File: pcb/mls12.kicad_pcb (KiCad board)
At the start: 4 copper layers, 130 x 40 mm, 137 parts, among them J1 MTJ-88ARX1-FSM-LG, J2 TC2070-FP, J3 SM04B-SRSS-TB, J4 JST B3B-ZR, J5 DC barrel plug, J6 JST B3B-ZR, J7 DC barrel plug, Q1 DMG3406L, Q2 DMG3406L, Q3 DMG3406L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

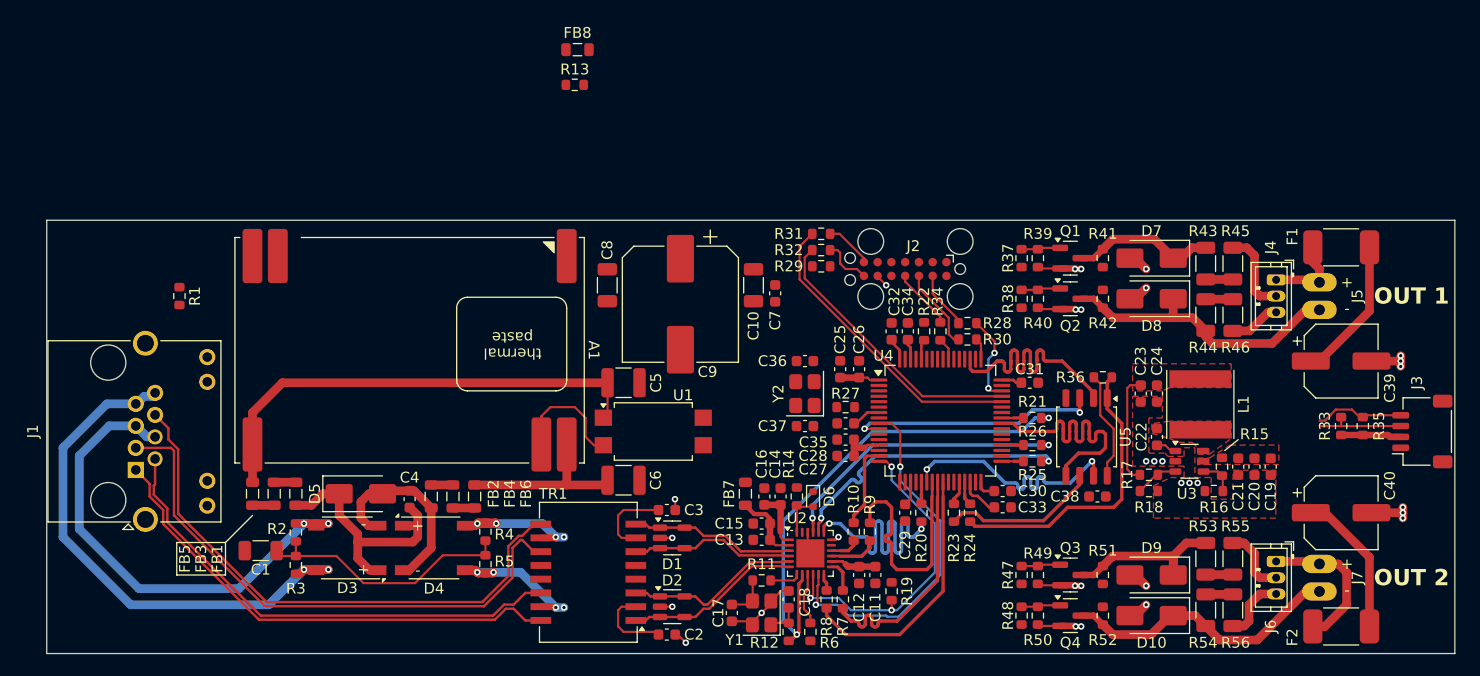
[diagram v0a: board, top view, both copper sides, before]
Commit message: Route +24V
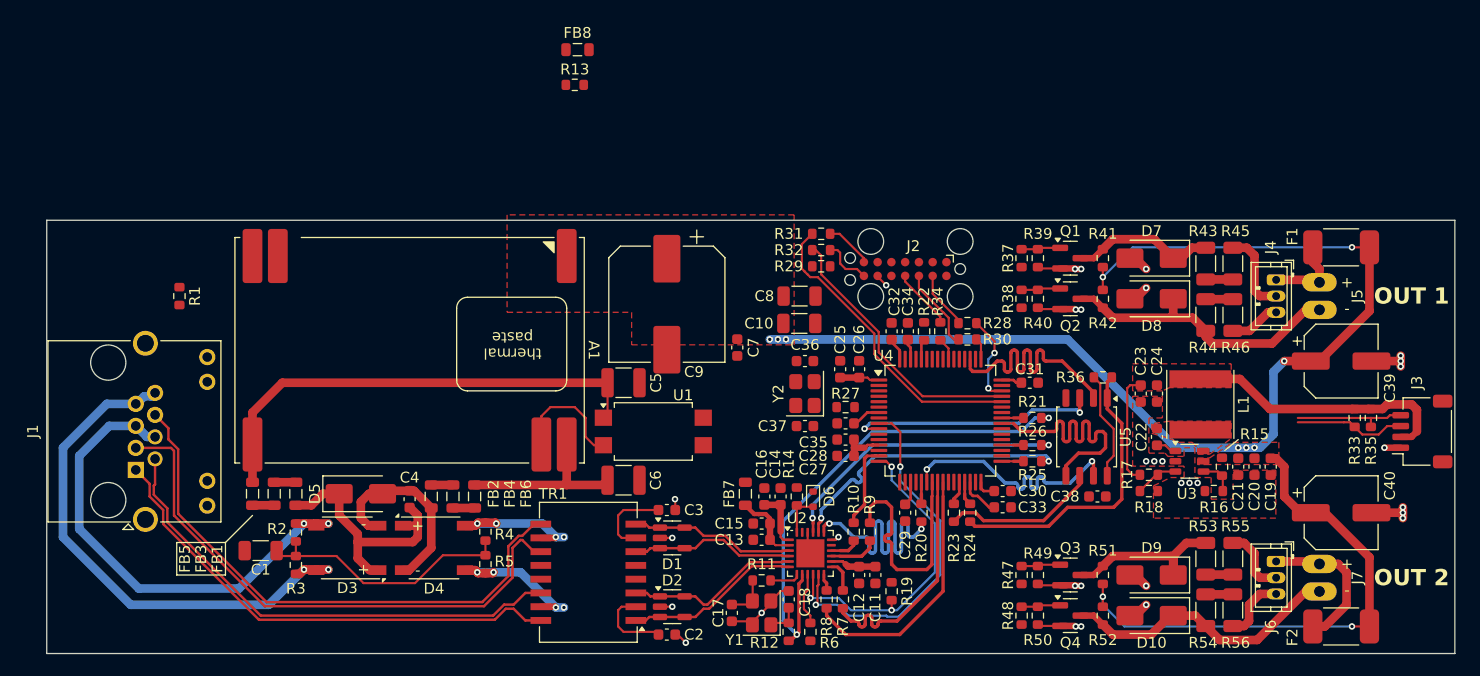
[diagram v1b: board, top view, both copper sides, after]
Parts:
- moved C8 17.8 mm to (179.5, 87.0), turned to 0 degrees
- moved C7 6.10 mm to (173.8, 91.8)
- moved C10 5.51 mm to (179.5, 89.5), turned to 0 degrees
- moved R33 1.46 mm to (230.8, 98.2), turned to -90 degrees
- moved C9 1.25 mm to (167.2, 87.8)
- moved R35 1.06 mm to (232.2, 98.2), turned to -90 degrees
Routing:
- net +24V: track 26.7 -> 151.0 mm, vias 0 -> 11
- net +3.3V: track 30.2 -> 49.8 mm
- net /MCU/SCL: track 8.30 -> 10.4 mm
- net /MCU/SDA: track 8.33 -> 10.3 mm
- net GND: track 44.3 -> 45.8 mm, vias 29 -> 30

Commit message: Route +3V3
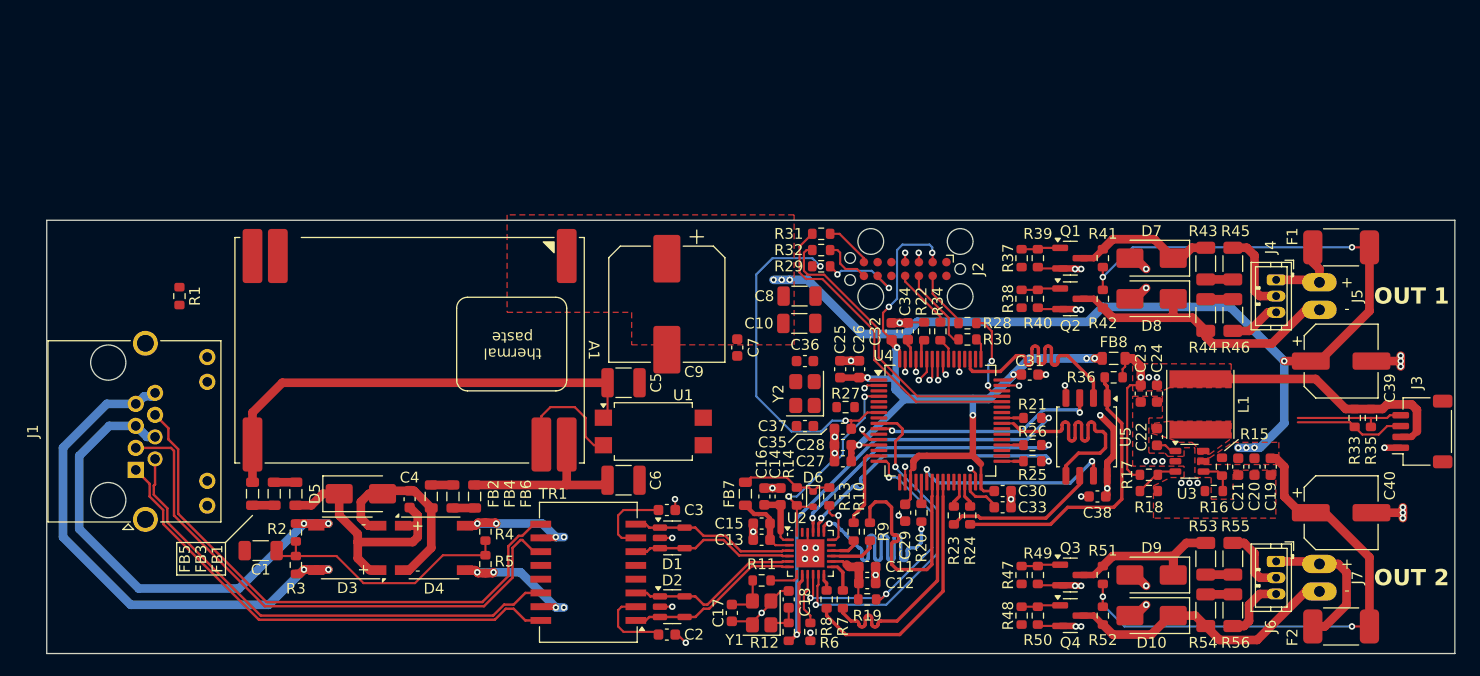
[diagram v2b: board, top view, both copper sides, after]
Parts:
- moved FB8 57.1 mm to (208.5, 92.8)
- moved R13 44.7 mm to (182.2, 105.5), turned to -90 degrees
- moved R19 2.37 mm to (185.8, 115.0), turned to 0 degrees
- moved C11 1.06 mm to (185.8, 112.0), turned to 0 degrees
- moved C12 1.06 mm to (185.8, 113.5), turned to 0 degrees
- moved R36 1.00 mm to (208.5, 94.5), turned to 180 degrees
- moved C31 0.75 mm to (200.8, 94.2)
- moved C27 0.56 mm to (183.5, 102.2)
- moved C28 0.56 mm to (183.5, 100.8)
- moved C35 0.56 mm to (183.5, 99.2)
- moved R23 0.25 mm to (193.8, 107.2)
- moved R24 0.25 mm to (195.2, 107.2)
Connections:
- U4 pad 20: /ETH-PHY/~{RST} -> unconnected-(U4A-PA4-Pad20)
- U4 pad 4: unconnected-(U4C-PC15-Pad4) -> /ETH-PHY/~{RST}
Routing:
- net /MCU/V_{t,ref}: track 15.7 -> 79.5 mm, vias 0 -> 9
- net /MCU/~{RESET}: track 2.71 -> 33.8 mm, vias 0 -> 2
- net GND: track 45.8 -> 72.8 mm, vias 30 -> 54
- net /ETH-PHY/~{RST}: track 4.04 -> 19.3 mm, vias 0 -> 2
- net +3.3V: track 49.8 -> 62.7 mm, vias 0 -> 5
- net Net-(J2-~{RESET}): track 1.19 -> 8.12 mm, vias 1 -> 2
- net +24V: track 151.0 -> 156.0 mm
- net /MCU/FLASH.IO_{3}: track 23.3 -> 19.3 mm
- net /ETH-PHY/INT: track 0.76 -> 4.38 mm
- net /MCU/FLASH.IO_{2}: track 23.4 -> 20.9 mm
- net /MCU/FLASH.IO_{0}: track 26.1 -> 23.7 mm
- net /MCU/FLASH.IO_{1}: track 24.9 -> 22.6 mm
- net /MCU/SDA: track 10.3 -> 12.5 mm, vias 0 -> 1
- net /MCU/SCL: track 10.4 -> 12.5 mm, vias 0 -> 1
- net /LED output 2/PWM_CW: track 0.00 -> 1.96 mm, vias 0 -> 1
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
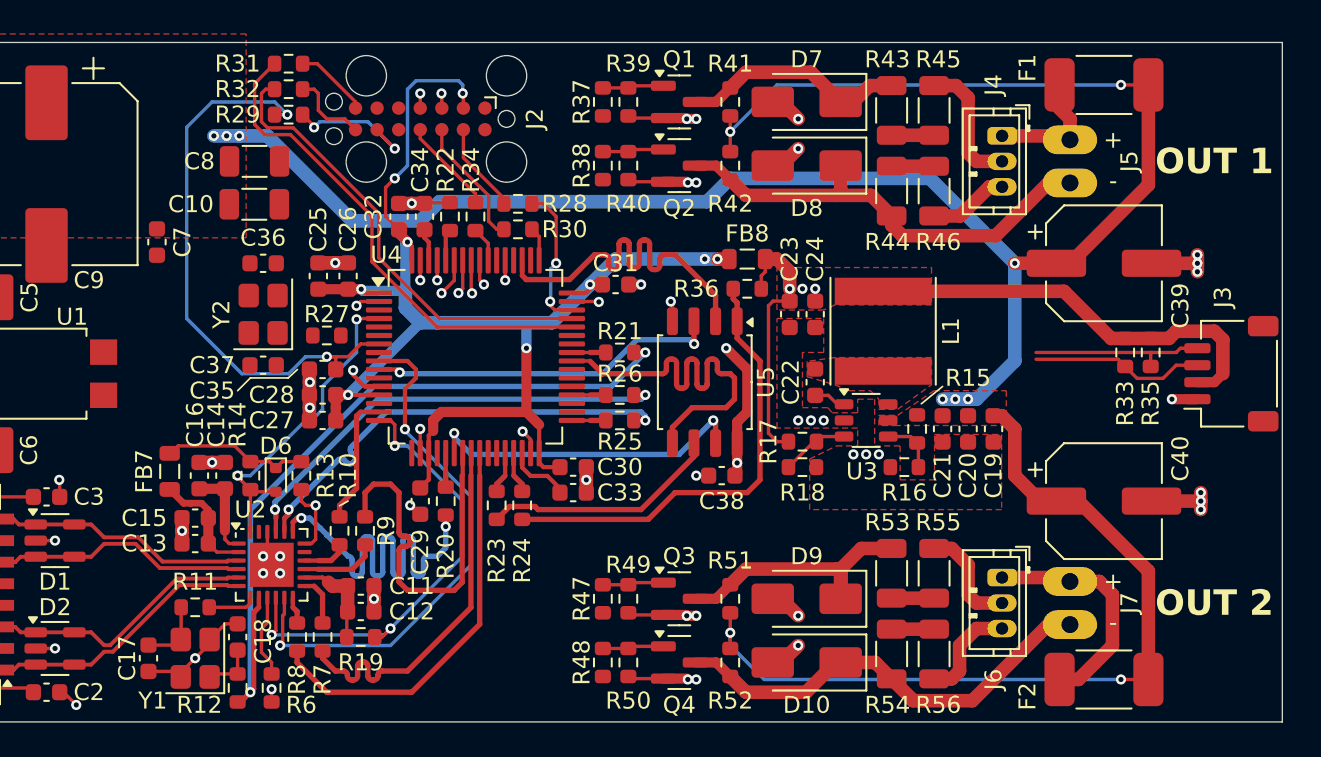
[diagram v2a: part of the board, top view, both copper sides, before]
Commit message: Route low-speed signals
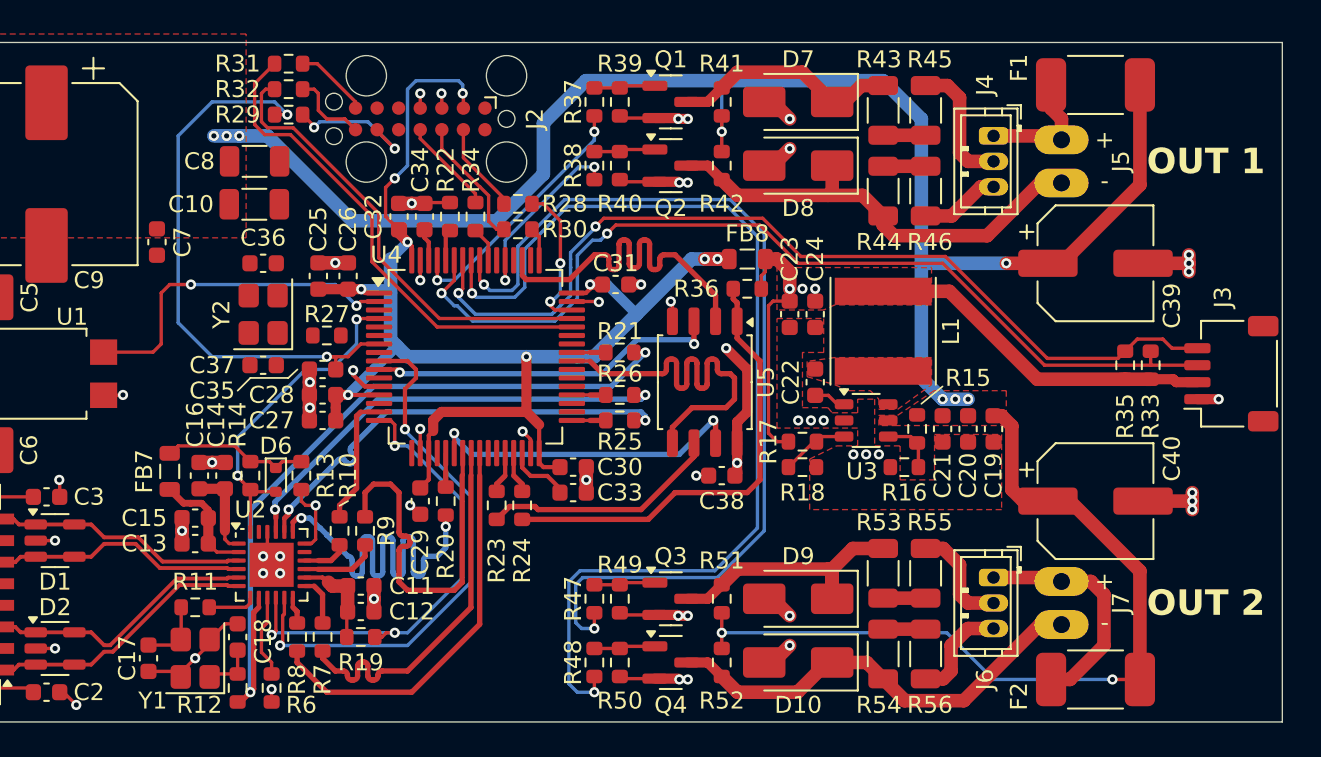
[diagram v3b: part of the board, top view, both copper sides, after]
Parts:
- moved R33 1.68 mm to (232.2, 99.0), turned to 90 degrees
- moved R35 1.68 mm to (230.8, 99.0), turned to 90 degrees
- moved C39 0.50 mm to (229.0, 93.0)
- moved C40 0.50 mm to (229.0, 107.0)
- moved D10 0.50 mm to (211.5, 116.5)
- moved D7 0.50 mm to (211.5, 83.5)
- moved D8 0.50 mm to (211.5, 87.2)
- moved D9 0.50 mm to (211.5, 112.8)
- moved F1 0.50 mm to (229.0, 82.5)
- moved F2 0.50 mm to (229.0, 117.5)
- moved J4 0.50 mm to (223.0, 85.5)
- moved J5 0.50 mm to (227.0, 87.0)
- moved J6 0.50 mm to (223.0, 111.5)
- moved J7 0.50 mm to (227.0, 113.0)
- moved Q1 0.50 mm to (204.0, 83.5)
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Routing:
- net /LED output 2/PWM_CW: track 1.96 -> 61.3 mm, vias 1 -> 2
- net /LED output 2/PWM_WW: track 1.53 -> 56.9 mm, vias 1 -> 2
- net /MCU/SDA: track 12.5 -> 55.5 mm, vias 1 -> 2
- net /MCU/SCL: track 12.5 -> 54.3 mm, vias 1 -> 2
- net /ETH-PoE+/TYP2_DET: track 1.43 -> 20.2 mm, vias 1 -> 2
- net /LED output 1/PWM_WW: track 1.17 -> 15.3 mm, vias 1 -> 2
- net +24V: track 156.0 -> 143.9 mm, vias 11 -> 10
- net /LED output 1/PWM_CW: track 1.17 -> 11.3 mm, vias 1 -> 2
- net +3.3V: track 62.7 -> 58.2 mm
- net /MCU/V_{t,ref}: track 79.5 -> 82.9 mm
- net GND: track 72.8 -> 73.7 mm, vias 54 -> 55
- net /ETH-PHY/MDIO: track 27.5 -> 28.3 mm
- net /ETH-PHY/MDC: track 31.9 -> 32.5 mm

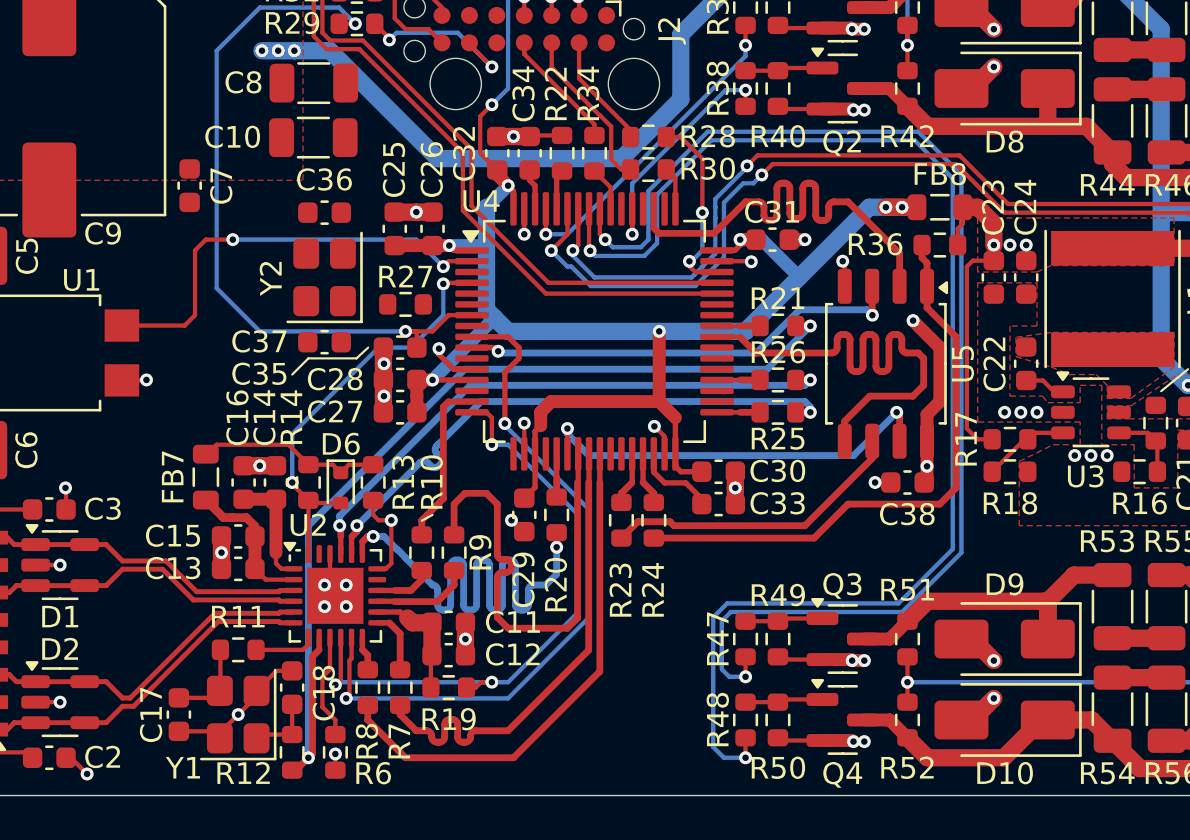
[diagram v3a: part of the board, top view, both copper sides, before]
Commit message: Route PHY +3V3
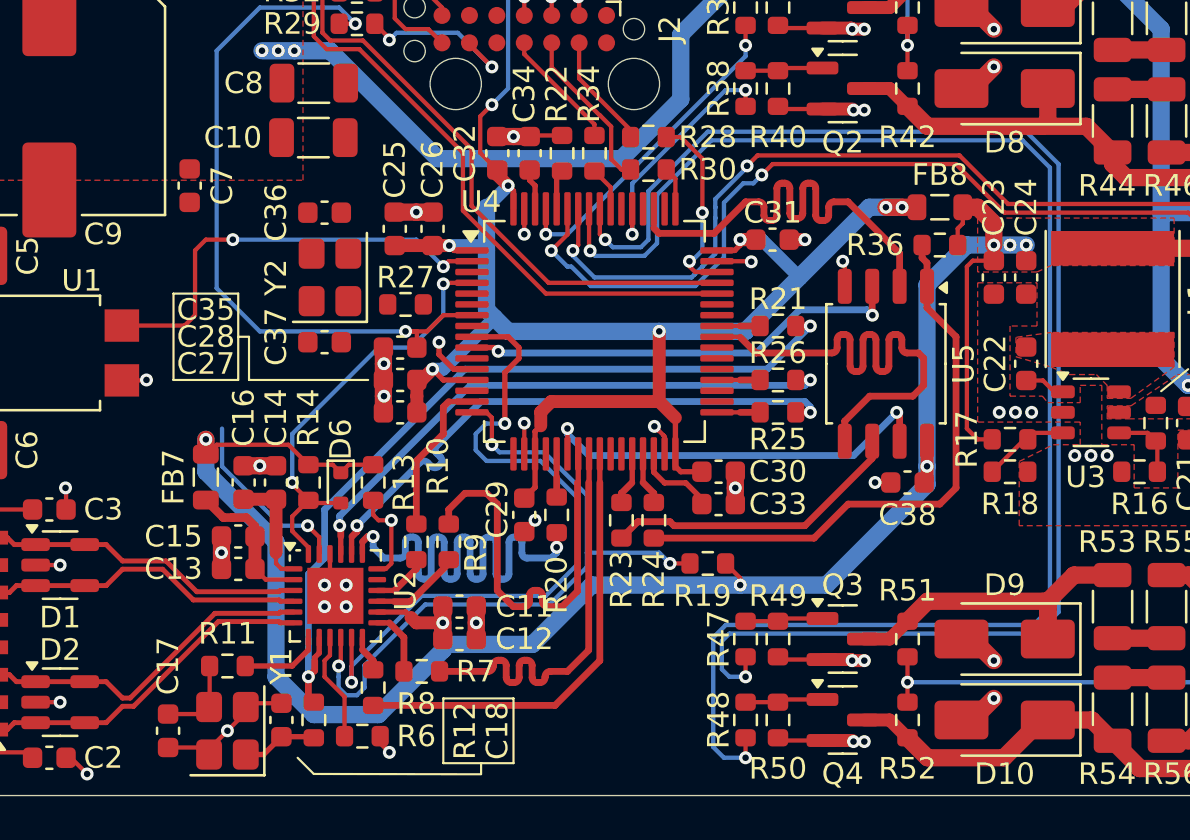
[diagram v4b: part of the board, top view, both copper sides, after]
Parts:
- moved R19 13.3 mm to (197.8, 109.2), turned to 180 degrees
- moved R12 1.80 mm to (179.5, 116.5), turned to -90 degrees
- moved C18 1.58 mm to (178.0, 116.5)
- moved R6 1.46 mm to (181.8, 117.2), turned to 0 degrees
- moved R7 1.25 mm to (184.5, 114.2), turned to 0 degrees
- moved C11 0.90 mm to (186.2, 111.2)
- moved C12 0.90 mm to (186.2, 112.8)
- moved C17 0.90 mm to (172.8, 117.0)
- moved R11 0.90 mm to (175.5, 114.0)
- moved Y1 0.90 mm to (175.5, 117.0)
- moved R10 0.56 mm to (184.2, 108.2)
- moved R9 0.56 mm to (185.8, 108.2)
- moved R8 0.25 mm to (182.2, 115.0)
- moved Y2 0.25 mm to (180.2, 96.0)
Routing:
- net +3.3V: track 58.2 -> 116.3 mm, vias 5 -> 7
- net /LED output 2/PWM_WW: track 56.9 -> 67.2 mm
- net /LED output 2/PWM_CW: track 61.3 -> 71.7 mm
- net /ETH-CONN/LED0: track 0.00 -> 8.39 mm, vias 0 -> 1
- net /ETH-PHY/CLK_25MHZ: track 45.3 -> 38.1 mm
- net /ETH-PHY/MDIO: track 28.3 -> 33.0 mm
- net /ETH-PHY/RXD_{1}: track 23.9 -> 20.9 mm
- net /ETH-PHY/RXD_{0}: track 22.4 -> 19.4 mm
- net /ETH-PHY/CRS_DV: track 21.7 -> 19.2 mm
- net Net-(U2-XO): track 2.84 -> 3.80 mm
- net /ETH-PHY/~{RST}: track 19.5 -> 20.1 mm

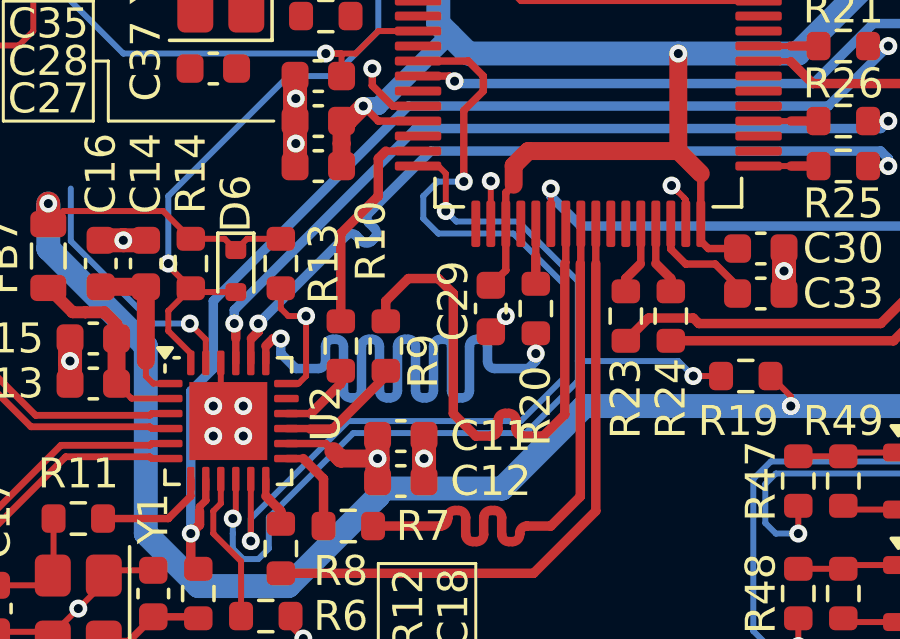
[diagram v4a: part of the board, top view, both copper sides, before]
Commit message: Route PHY IRQ
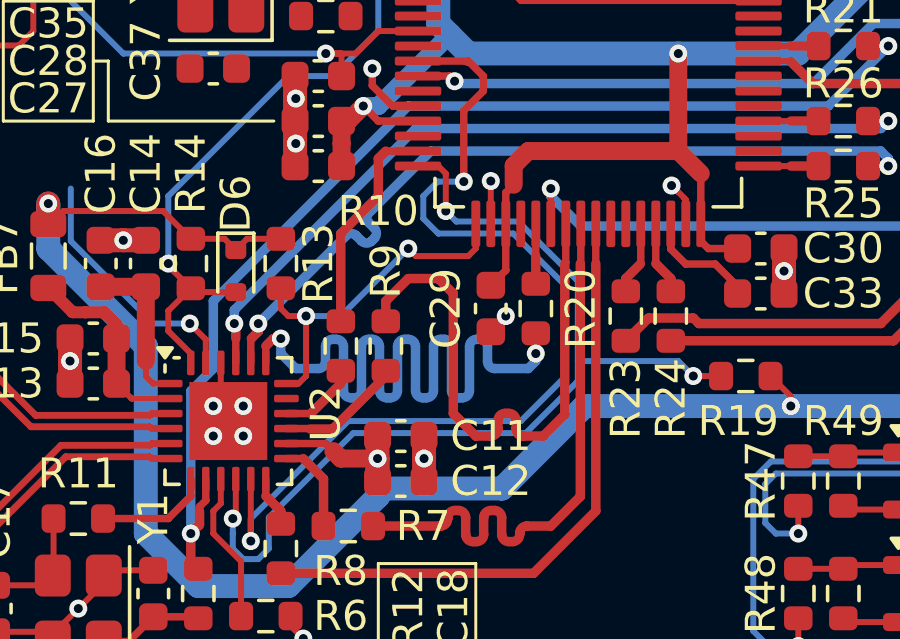
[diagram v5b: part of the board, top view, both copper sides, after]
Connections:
- U4 pad 17: unconnected-(U4A-PA3-Pad17) -> /ETH-PHY/INT
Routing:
- net /ETH-PHY/INT: track 4.38 -> 12.0 mm, vias 1 -> 2
